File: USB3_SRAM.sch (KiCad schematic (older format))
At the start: 0 parts

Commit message: Added USB3 SRAM Added 5V regulator
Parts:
- added C?: C_Small, Capacitor_SMD:C_0603_1608Metric_Pad1.08x0.95mm_HandSolder, symbol Device:C_Small
- added C?: C_Polarized_Small, Capacitor_Tantalum_SMD:CP_EIA-1608-10_AVX-L_Pad1.25x1.05mm_HandSolder, symbol Device:C_Polarized_Small
- added C?: C_Small, symbol Device:C_Small
- added C? (x24): 100nF, Capacitor_SMD:C_0603_1608Metric_Pad1.08x0.95mm_HandSolder, symbol Device:C_Small
- added IC? (x2): CY7C1062GE30-10BGXI, BGA119C127P7X17_1400X2200X240, symbol GM_Memory_RAM:CY7C1062GE30-10BGXI
- added R? (x2): R_Small_US, Resistor_SMD:R_0603_1608Metric_Pad0.98x0.95mm_HandSolder, symbol Device:R_Small_US
- added R?: 2K, Resistor_SMD:R_0603_1608Metric_Pad0.98x0.95mm_HandSolder, symbol Device:R_Small_US
- added R? (x3): 10K, Resistor_SMD:R_0603_1608Metric_Pad0.98x0.95mm_HandSolder, symbol Device:R_Small_US
- added R? (x3): 0, Resistor_SMD:R_0603_1608Metric_Pad0.98x0.95mm_HandSolder, symbol Device:R_Small_US
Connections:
- new net: IC?.B2 (A18), IC?.B3 (A17), IC?.B5 (A16), IC?.B6 (A15), IC?.C2 (~BC), IC?.C3 (~CE2), IC?.C5 (~CE3), IC?.C6 (~BA), IC?.R2 (A14), IC?.R3 (~BD), IC?.R5 (~BB), IC?.R6 (A13), IC?.T2 (A12), IC?.T3 (A11), IC?.T5 (A10), IC?.T6 (A9), IC?.U2 (A8), R?.1
- new net: IC?.B4 (~CE1), R?.1, R?.2
- new net: IC?.T4 (~WE), R?.1, R?.2
- new net: IC?.U4 (~OE), R?.1, R?.2
- new net CTL0: R?.2
- new net CTL1: R?.2
- new net CTL10: IC?.U6 (A5)
- new net CTL11: IC?.U5 (A6)
- new net CTL12: IC?.U3 (A7)
- new net CTL2: R?.2
- new net CTL5: IC?.A6 (A0)
- new net CTL6: IC?.A5 (A1)
- new net CTL7: IC?.A4 (A2)
- new net CTL8: IC?.A3
- new net CTL9: IC?.A2 (A4)
- new net GNDD: C?.2, C?.2, C?.2, C?.2, C?.2, C?.2, C?.2, C?.2, C?.2, C?.2, C?.2, C?.2, C?.2, C?.2, C?.2, C?.2, C?.2, C?.2, C?.2, C?.2, C?.2, C?.2, C?.2, C?.2, IC?.D3 (VSS_1), IC?.D4 (VSS_2), IC?.D5 (VSS_3), IC?.E2 (VSS_4), IC?.E4 (VSS_5), IC?.E6 (VSS_6), IC?.F3 (VSS_7), IC?.F4 (VSS_8), IC?.F5 (VSS_9), IC?.G2 (VSS_10), IC?.G4 (VSS_11), IC?.G6 (VSS_12), IC?.H3 (VSS_13), IC?.H4 (VSS_14), IC?.H5 (VSS_15), IC?.J2 (VSS_16), IC?.J4 (VSS_17), IC?.J6 (VSS_18), IC?.K3 (VSS_19), IC?.K4 (VSS_20), IC?.K5 (VSS_21), IC?.L2 (VSS_22), IC?.L4 (VSS_23), IC?.L6 (VSS_24), IC?.M3 (VSS_25), IC?.M4 (VSS_26), IC?.M5 (VSS_27), IC?.N2 (VSS_28), IC?.N4 (VSS_29), IC?.N6 (VSS_30), IC?.P3 (VSS_31), IC?.P4 (VSS_32), IC?.P5 (VSS_33), R?.2
- new net V3P3: C?.1, C?.1, C?.1, C?.1, C?.1, C?.1, C?.1, C?.1, C?.1, C?.1, C?.1, C?.1, C?.1, C?.1, C?.1, C?.1, C?.1, C?.1, C?.1, C?.1, C?.1, C?.1, C?.1, C?.1, IC?.D2 (VDD_1), IC?.D6 (VDD_2), IC?.E3 (VDD_3), IC?.E5 (VDD_4), IC?.F2 (VDD_5), IC?.F6 (VDD_6), IC?.G3 (VDD_7), IC?.G5 (VDD_8), IC?.H2 (VDD_9), IC?.H6 (VDD_10), IC?.J3 (VDD_11), IC?.J5 (VDD_12), IC?.K2 (VDD_13), IC?.K6 (VDD_14), IC?.L3 (VDD_15), IC?.L5 (VDD_16), IC?.M2 (VDD_17), IC?.M6 (VDD_18), IC?.N3 (VDD_19), IC?.N5 (VDD_20), IC?.P2 (VDD_21), IC?.P6 (VDD_22), R?.1, R?.1, R?.1
- no-connect marks 0 -> 4

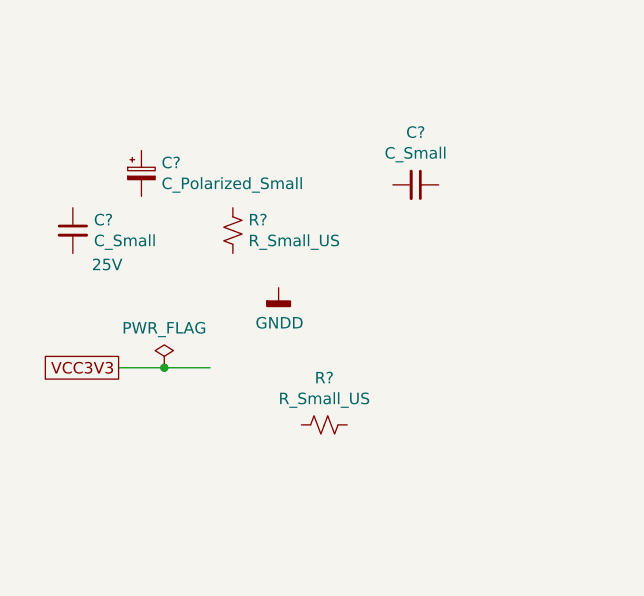
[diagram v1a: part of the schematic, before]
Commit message: Added USB3 type B connector Added ESD protection to the same sheet
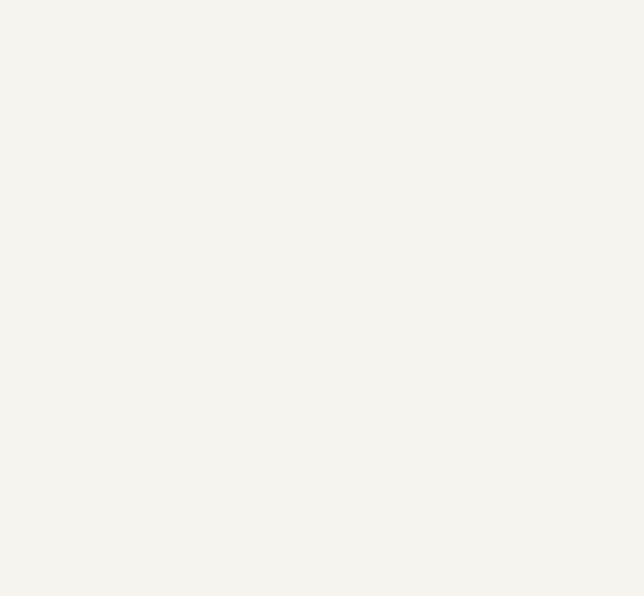
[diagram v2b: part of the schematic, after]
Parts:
- removed C?: C_Small, Capacitor_SMD:C_0603_1608Metric_Pad1.08x0.95mm_HandSolder, symbol Device:C_Small
- removed C?: C_Polarized_Small, Capacitor_Tantalum_SMD:CP_EIA-1608-10_AVX-L_Pad1.25x1.05mm_HandSolder, symbol Device:C_Polarized_Small
- removed C?: C_Small, symbol Device:C_Small
- removed R? (x2): R_Small_US, Resistor_SMD:R_0603_1608Metric_Pad0.98x0.95mm_HandSolder, symbol Device:R_Small_US
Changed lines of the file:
@@
-$Comp
-L Device:R_Small_US R?
-U 1 1 603A5B6D
-P -1450 1550
-AR Path="/601E7C5A/603A5B6D" Ref="R?"  Part="1"
-AR Path="/601E7CC8/603A5B6D" Ref="R?"  Part="1"
-AR Path="/601E7C92/603A5B6D" Ref="R?"  Part="1"
-AR Path="/601E7C92/60257FE5/603A5B6D" Ref="R?"  Part="1"
-AR Path="/601E7B38/603A5B6D" Ref="R?"  Part="1"
-AR Path="/60256C5F/603A5B6D" Ref="R?"  Part="1"
-AR Path="/601E7BBE/60277424/603A5B6D" Ref="R?"  Part="1"
-AR Path="/601E7BBE/603A73D8/603A5B6D" Ref="R?"  Part="1"
-F 0 "R?" H -1382 1596 50  0000 L CNN
-F 1 "R_Small_US" H -1382 1505 50  0000 L CNN
-F 2 "Resistor_SMD:R_0603_1608Metric_Pad0.98x0.95mm_HandSolder" H -1450 1550 50  0001 C CNN
-F 3 "~" H -1450 1550 50  0001 C CNN
-	1    -1450 1550
-	1    0    0    -1
-$EndComp
-$Comp
-L Device:C_Small C?
-U 1 1 603A5B74
-P -2150 1550
-AR Path="/601E7C5A/603A5B74" Ref="C?"  Part="1"
-AR Path="/601E7CC8/603A5B74" Ref="C?"  Part="1"
-AR Path="/601E7C92/603A5B74" Ref="C?"  Part="1"
-AR Path="/601E7C92/60257FE5/603A5B74" Ref="C?"  Part="1"
-AR Path="/601E7B38/603A5B74" Ref="C?"  Part="1"
-AR Path="/60256C5F/603A5B74" Ref="C?"  Part="1"
-AR Path="/601E7BBE/60277424/603A5B74" Ref="C?"  Part="1"
-AR Path="/601E7BBE/603A73D8/603A5B74" Ref="C?"  Part="1"
-F 0 "C?" H -2058 1596 50  0000 L CNN
-F 1 "C_Small" H -2058 1505 50  0000 L CNN
-F 2 "Capacitor_SMD:C_0603_1608Metric_Pad1.08x0.95mm_HandSolder" H -2150 1550 50  0001 C CNN
-F 3 "~" H -2150 1550 50  0001 C CNN
-F 4 "25V" H -2000 1400 50  0000 C CNN "Voltage"
-	1    -2150 1550
-	1    0    0    -1
-$EndComp
-Text GLabel -1950 2150 0    50   UnSpc ~ 0
-VCC3V3
-$Comp
-L power:PWR_FLAG #FLG?
-U 1 1 603A5B7B
-P -1750 2150
-AR Path="/601E7C5A/603A5B7B" Ref="#FLG?"  Part="1"
-AR Path="/601E7CC8/603A5B7B" Ref="#FLG?"  Part="1"
-AR Path="/601E7C92/603A5B7B" Ref="#FLG?"  Part="1"
-AR Path="/601E7C92/60257FE5/603A5B7B" Ref="#FLG?"  Part="1"
-AR Path="/601E7B38/603A5B7B" Ref="#FLG?"  Part="1"
-AR Path="/60256C5F/603A5B7B" Ref="#FLG?"  Part="1"
-AR Path="/601E7BBE/60277424/603A5B7B" Ref="#FLG?"  Part="1"
-AR Path="/601E7BBE/603A73D8/603A5B7B" Ref="#FLG?"  Part="1"
-F 0 "#FLG?" H -1750 2225 50  0001 C CNN
-F 1 "PWR_FLAG" H -1750 2323 50  0000 C CNN
-F 2 "" H -1750 2150 50  0001 C CNN
-F 3 "~" H -1750 2150 50  0001 C CNN
-	1    -1750 2150
-	1    0    0    -1
-$EndComp
-Connection ~ -1750 2150
-Wire Wire Line
-	-1750 2150 -1550 2150
-Wire Wire Line
-	-1950 2150 -1750 2150
-$Comp
-L power:GNDD #PWR?
-U 1 1 603A5B84
-P -1250 1800
-AR Path="/601DF0A6/603A5B84" Ref="#PWR?"  Part="1"
-AR Path="/601E7C5A/603A5B84" Ref="#PWR?"  Part="1"
-AR Path="/601E7CC8/603A5B84" Ref="#PWR?"  Part="1"
-AR Path="/601E7C92/603A5B84" Ref="#PWR?"  Part="1"
-AR Path="/601E7C92/60257FE5/603A5B84" Ref="#PWR?"  Part="1"
-AR Path="/601E7B38/603A5B84" Ref="#PWR?"  Part="1"
-AR Path="/60256C5F/603A5B84" Ref="#PWR?"  Part="1"
-AR Path="/601E7BBE/60277424/603A5B84" Ref="#PWR?"  Part="1"
-AR Path="/601E7BBE/603A73D8/603A5B84" Ref="#PWR?"  Part="1"
-F 0 "#PWR?" H -1250 1550 50  0001 C CNN
-F 1 "GNDD" H -1246 1645 50  0000 C CNN
-F 2 "" H -1250 1800 50  0001 C CNN
-F 3 "" H -1250 1800 50  0001 C CNN
-	1    -1250 1800
-	1    0    0    -1
-$EndComp
-$Comp
-L Device:C_Polarized_Small C?
-U 1 1 603A5B8B
-P -1850 1300
-AR Path="/601E7C92/603A5B8B" Ref="C?"  Part="1"
-AR Path="/601E7C92/60257FE5/603A5B8B" Ref="C?"  Part="1"
-AR Path="/601E7B38/603A5B8B" Ref="C?"  Part="1"
-AR Path="/60256C5F/603A5B8B" Ref="C?"  Part="1"
-AR Path="/601E7BBE/60277424/603A5B8B" Ref="C?"  Part="1"
-AR Path="/601E7BBE/603A73D8/603A5B8B" Ref="C?"  Part="1"
-F 0 "C?" H -1762 1346 50  0000 L CNN
-F 1 "C_Polarized_Small" H -1762 1255 50  0000 L CNN
-F 2 "Capacitor_Tantalum_SMD:CP_EIA-1608-10_AVX-L_Pad1.25x1.05mm_HandSolder" H -1850 1300 50  0001 C CNN
-F 3 "~" H -1850 1300 50  0001 C CNN
-F 4 "" H -1850 1300 50  0000 C CNN "Voltage"
-	1    -1850 1300
-	1    0    0    -1
-$EndComp
-$Comp
-L Device:C_Small C?
-U 1 1 603A5B91
-P -650 1350
-AR Path="/601E7B38/603A5B91" Ref="C?"  Part="1"
-AR Path="/60256C5F/603A5B91" Ref="C?"  Part="1"
-AR Path="/601E7BBE/60277424/603A5B91" Ref="C?"  Part="1"
-AR Path="/601E7BBE/603A73D8/603A5B91" Ref="C?"  Part="1"
-F 0 "C?" V -879 1350 50  0000 C CNN
-F 1 "C_Small" V -788 1350 50  0000 C CNN
-F 2 "" H -650 1350 50  0001 C CNN
-F 3 "~" H -650 1350 50  0001 C CNN
-	1    -650 1350
-	0    1    1    0
-$EndComp
-$Comp
-L Device:R_Small_US R?
-U 1 1 603A5B97
-P -1050 2400
-AR Path="/60256C5F/603A5B97" Ref="R?"  Part="1"
-AR Path="/601E7BBE/60277424/603A5B97" Ref="R?"  Part="1"
-AR Path="/601E7BBE/603A73D8/603A5B97" Ref="R?"  Part="1"
-F 0 "R?" V -1255 2400 50  0000 C CNN
-F 1 "R_Small_US" V -1164 2400 50  0000 C CNN
-F 2 "Resistor_SMD:R_0603_1608Metric_Pad0.98x0.95mm_HandSolder" H -1050 2400 50  0001 C CNN
-F 3 "~" H -1050 2400 50  0001 C CNN
-	1    -1050 2400
-	0    1    1    0
-$EndComp
 $Comp
 L Device:R_Small_US R?
